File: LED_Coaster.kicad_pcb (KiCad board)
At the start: 2 copper layers, 90 x 90 mm, 60 parts, among them J1 USB_C_Receptacle_USB2.0, SW1 SW_Push, SW2 SW_DIP_x01, SW3 SW_DIP_x01, U1 ATmega32U4-A, Y1 Crystal_GND24

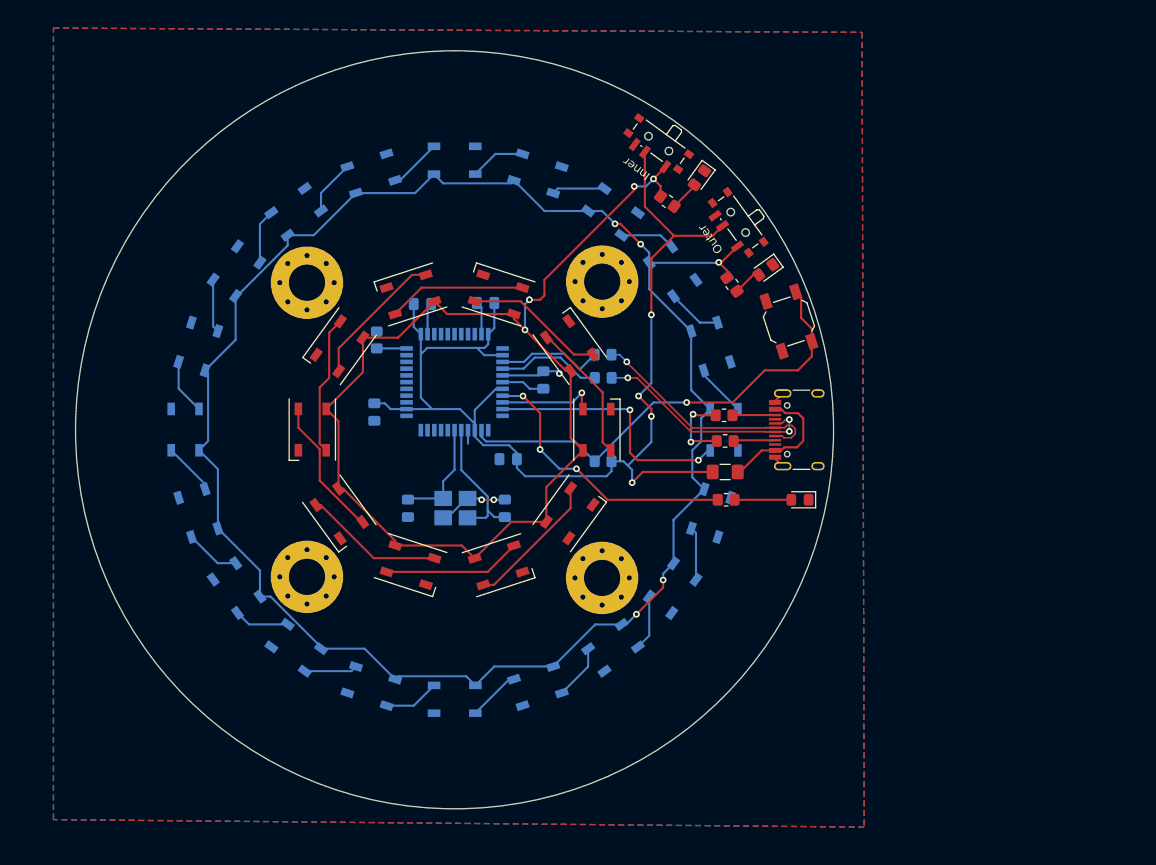
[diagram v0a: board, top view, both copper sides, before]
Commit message: Added more components
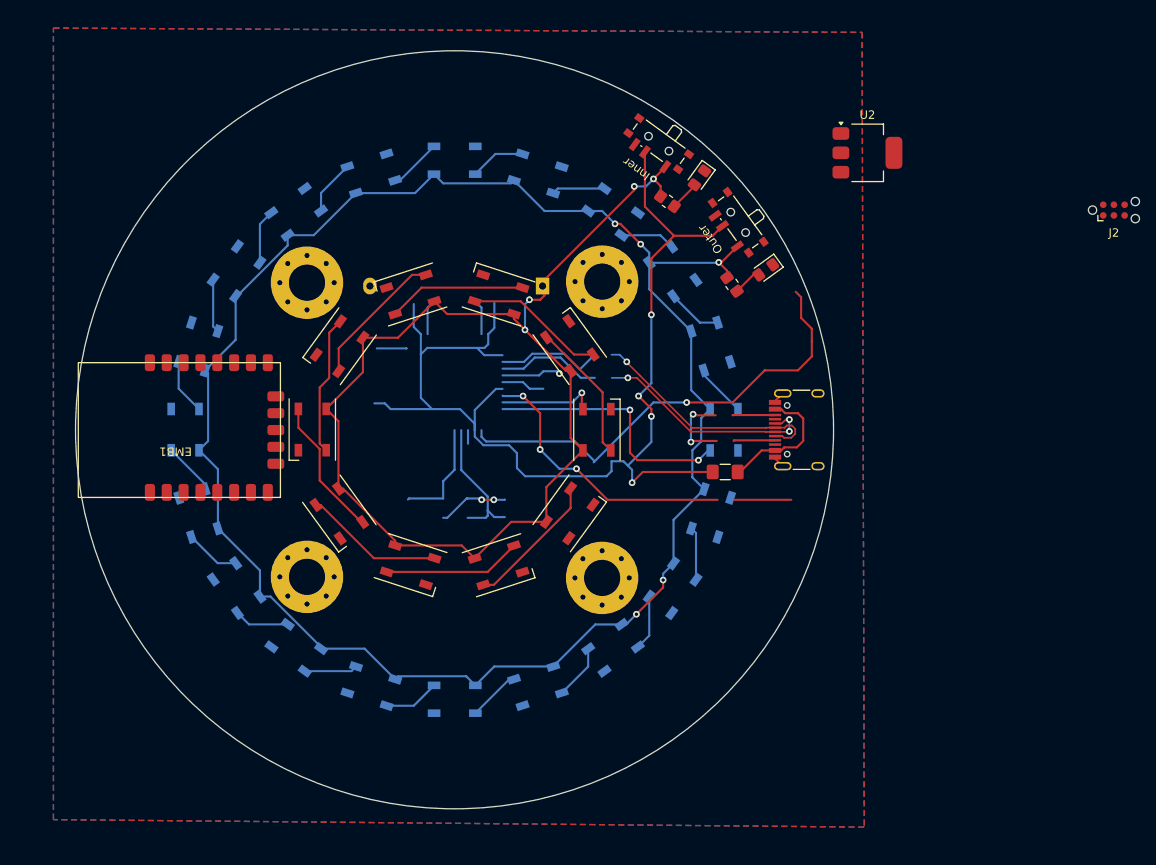
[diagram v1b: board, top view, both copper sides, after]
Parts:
- removed C1: 1uF, Capacitor_SMD:C_0805_2012Metric_Pad1.18x1.45mm_HandSolder
- removed C2: 10uF, Capacitor_SMD:C_0805_2012Metric_Pad1.18x1.45mm_HandSolder
- removed C3, C4, C5: 0.1uF, Capacitor_SMD:C_0805_2012Metric_Pad1.18x1.45mm_HandSolder
- removed C6, C7: 22pF, Capacitor_SMD:C_0805_2012Metric_Pad1.18x1.45mm_HandSolder
- removed D33: LED, LED_SMD:LED_0805_2012Metric_Pad1.15x1.40mm_HandSolder
- removed R1, R4: 10K, Resistor_SMD:R_0805_2012Metric_Pad1.20x1.40mm_HandSolder
- removed R2, R3: 22, Resistor_SMD:R_0805_2012Metric_Pad1.20x1.40mm_HandSolder
- removed R5, R6: 5.1K, Resistor_SMD:R_0805_2012Metric_Pad1.20x1.40mm_HandSolder
- removed R9: 150, Resistor_SMD:R_0805_2012Metric_Pad1.20x1.40mm_HandSolder
- removed SW1: SW_Push, Button_Switch_SMD:SW_SPST_SKQG_WithoutStem
- removed U1: ATmega32U4-A, Package_QFP:TQFP-44_10x10mm_P0.8mm
- removed Y1: Crystal_GND24, Crystal:Crystal_SMD_3225-4Pin_3.2x2.5mm_HandSoldering
- added BT1: Battery_Cell, Battery:Battery_Panasonic_CR2032-HFN_Horizontal_CircularHoles, B.Cu at (160.4, 62.9)
- added EMB1: ~, Library:EMB1082, F.Cu at (116.9, 80.0)
- added J2: Conn_ARM_SWD_TagConnect_TC2030-NL, Connector:Tag-Connect_TC2030-IDC-NL_2x03_P1.27mm_Vertical, F.Cu at (228.3, 53.9)
- added U2: LD1117S33TR_SOT223, Package_TO_SOT_SMD:SOT-223-3_TabPin2, F.Cu at (199.0, 47.1)
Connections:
- J1 pad A5: Net-(J1-CC1) -> unconnected-(J1-CC1-PadA5)
- J1 pad A6: /D+ -> unconnected-(J1-D+-PadA6)
- J1 pad A7: /D- -> unconnected-(J1-D--PadA7)
- J1 pad B5: Net-(J1-CC2) -> unconnected-(J1-CC2-PadB5)
- J1 pad B6: /D+ -> unconnected-(J1-D+-PadB6)
- J1 pad B7: /D- -> unconnected-(J1-D--PadB7)
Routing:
- net (no net): track 0.00 -> 159.3 mm, vias 0 -> 7
- net Net-(U1-~{RESET}): track 55.0 -> 0.00 mm, vias 1 -> 0
- net /small_ring: track 11.9 -> 66.9 mm, vias 1 -> 2
- net Net-(U1-PB0): track 33.2 -> 0.00 mm, vias 3 -> 0
- net /D-: track 29.0 -> 0.00 mm, vias 1 -> 0
- net /D+: track 27.1 -> 0.00 mm, vias 3 -> 0
- net Net-(U1-XTAL2): track 16.3 -> 0.00 mm
- net Net-(U1-XTAL1): track 12.9 -> 0.00 mm
- net Net-(U1-D-): track 12.8 -> 0.00 mm
- net Net-(U1-D+): track 12.5 -> 0.00 mm
- net Net-(D33-A): track 6.74 -> 0.00 mm
- net Net-(U1-UCAP): track 5.17 -> 0.00 mm
- net unconnected-(J1-CC2-PadB5): track 0.00 -> 5.06 mm
- net Net-(J1-CC2): track 5.06 -> 0.00 mm
- net unconnected-(J1-CC1-PadA5): track 0.00 -> 4.95 mm
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
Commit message: Added traces for EMB1082 and power switch
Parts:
- removed BT1: Battery_Cell, Battery:Battery_Panasonic_CR2032-HFN_Horizontal_CircularHoles
- removed F1: Polyfuse, Fuse:Fuse_1206_3216Metric_Pad1.42x1.75mm_HandSolder
- removed J1: USB_C_Receptacle_USB2.0, Connector_USB:USB_C_Receptacle_HRO_TYPE-C-31-M-12
- added 5V: TestPoint, TestPoint:TestPoint_Loop_D1.80mm_Drill1.0mm_Beaded, F.Cu at (190.5, 77.5)
- added D33: LED, LED_SMD:LED_0805_2012Metric_Pad1.15x1.40mm_HandSolder, F.Cu at (191.5, 73.5)
- added GND: TestPoint, TestPoint:TestPoint_Loop_D1.80mm_Drill1.0mm_Beaded, F.Cu at (190.6, 82.4)
- added Power: SW_DIP_x01, Button_Switch_SMD:SW_SPDT_PCM12, F.Cu at (189.6, 68.1)
- added R1: 150, Resistor_SMD:R_0805_2012Metric_Pad1.20x1.40mm_HandSolder, F.Cu at (185.8, 69.8)
- moved J2 112.5 mm to (116.4, 65.3), turned to 180 degrees
- moved U2 92.0 mm to (121.5, 96.6), turned to 90 degrees
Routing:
- net (no net): track 159.3 -> 0.00 mm, vias 7 -> 0
- net +5V: track 135.2 -> 69.2 mm, vias 4 -> 7
- net 3.3V: track 0.00 -> 43.6 mm, vias 0 -> 2
- net /large_ring: track 30.8 -> 60.1 mm, vias 2 -> 1
- net Net-(EMB1-#RESET): track 0.00 -> 29.2 mm
- net /small_ring: track 66.9 -> 37.9 mm
- net Net-(EMB1-SWD_IO): track 0.00 -> 22.8 mm, vias 0 -> 2
- net Net-(EMB1-SWD_CLK): track 0.00 -> 21.3 mm
- net Net-(F1-Pad2): track 15.8 -> 0.00 mm
- net Net-(SW1-Pad1): track 0.00 -> 7.76 mm, vias 0 -> 1
- net Net-(D1-VDD): track 218.3 -> 211.3 mm, vias 5 -> 9
- net Net-(D33-A): track 0.00 -> 5.68 mm
- net unconnected-(J1-CC2-PadB5): track 5.06 -> 0.00 mm
- net unconnected-(J1-CC1-PadA5): track 4.95 -> 0.00 mm
- net GND: track 37.8 -> 35.2 mm, vias 5 -> 16
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- added copper zone on F.Cu, net +5V
